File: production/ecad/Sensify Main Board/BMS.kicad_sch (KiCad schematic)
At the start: 76 parts, among them J1 1-2834011-3, J2 1-2834011-2, Q1 2N700, Q2 PMPB13XNE,115, Q3 PMPB13XNE,115, Q4 BSS223PWH6327XTSA1, U1 MAX17320G22, U2 BQ25306RTER, U3 LD29150DT33R, U4 LM22676MRX-5.0_NOPB

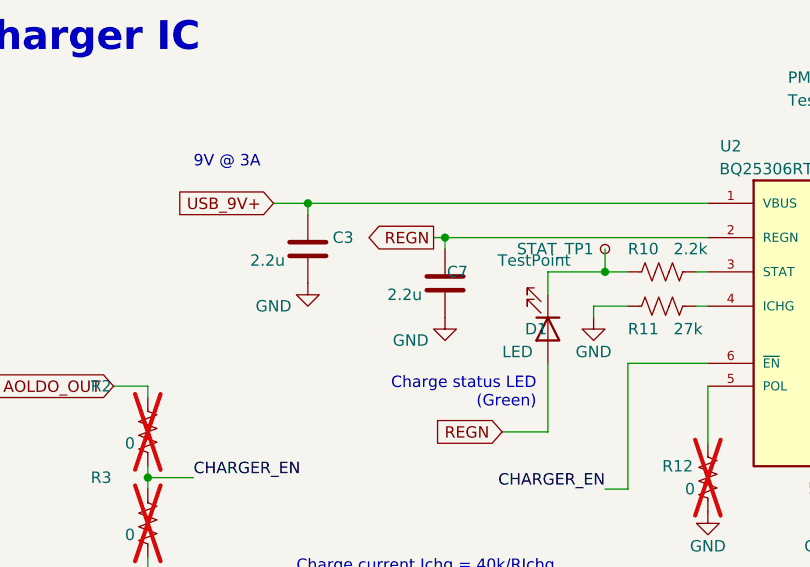
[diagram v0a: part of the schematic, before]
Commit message: added C16 footprint BMS
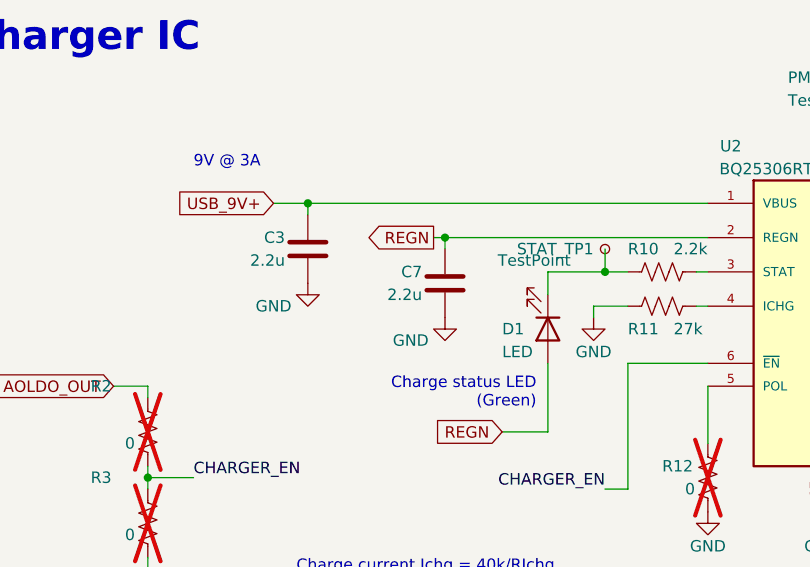
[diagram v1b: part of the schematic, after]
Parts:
- C16: footprint (none) -> Capacitor_SMD:C_0603_1608Metric_Pad1.08x0.95mm_HandSolder
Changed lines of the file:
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@@
   (symbol (lib_id "Device:C") (at 53.34 200.66 0) (unit 1)
     (in_bom yes) (on_board yes) (dnp no)
-    (property "Reference" "C3" (at 58.42 199.39 0)
+    (property "Reference" "C3" (at 50.8 199.39 0)
       (effects (font (size 1.27 1.27)) (justify right))
     )
@@
       (effects (font (size 1.27 1.27)) (justify right))
     )
-    (property "Footprint" "" (at 237.1852 209.55 0)
+    (property "Footprint" "Capacitor_SMD:C_0603_1608Metric_Pad1.08x0.95mm_HandSolder" (at 237.1852 209.55 0)
       (effects (font (size 1.27 1.27)) hide)
     )
@@
   (symbol (lib_id "Device:LED") (at 80.01 209.55 270) (unit 1)
     (in_bom yes) (on_board yes) (dnp no)
-    (property "Reference" "D1" (at 77.47 209.55 90)
+    (property "Reference" "D1" (at 74.93 209.55 90)
       (effects (font (size 1.27 1.27)) (justify left))
     )
@@
   (symbol (lib_id "Device:C") (at 68.58 204.47 0) (unit 1)
     (in_bom yes) (on_board yes) (dnp no)
-    (property "Reference" "C7" (at 71.12 203.2 0)
-      (effects (font (size 1.27 1.27)) (justify right))
-    )
+    (property "Reference" "C7" (at 66.04 203.2 0)
+      (effects (font (size 1.27 1.27)) (justify right))
+    )

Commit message: updated footprints for U3, U4
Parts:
- U3: footprint BMS:DPAK456P972X240-3N -> Sensify Footprints:DPAK456P972X240-3N
- U4: footprint LM22676MRX-5.0_NOPB:VREG_LM5017MR_NOPB -> Sensify Footprints:VREG_LM5017MR_NOPB
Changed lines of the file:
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@@
       (effects (font (size 1.27 1.27)))
     )
-    (property "Footprint" "LM22676MRX-5.0_NOPB:VREG_LM5017MR_NOPB" (at 303.53 115.57 0)
+    (property "Footprint" "Sensify Footprints:VREG_LM5017MR_NOPB" (at 303.53 115.57 0)
       (effects (font (size 1.27 1.27)) (justify bottom) hide)
     )
@@
       (effects (font (size 1.27 1.27)))
     )
-    (property "Footprint" "BMS:DPAK456P972X240-3N" (at 256.54 203.2 0)
+    (property "Footprint" "Sensify Footprints:DPAK456P972X240-3N" (at 256.54 203.2 0)
       (effects (font (size 1.27 1.27)) (justify bottom) hide)
     )

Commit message: reannotated REFDES
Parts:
- renumbered C7 to C6, C6 to C7

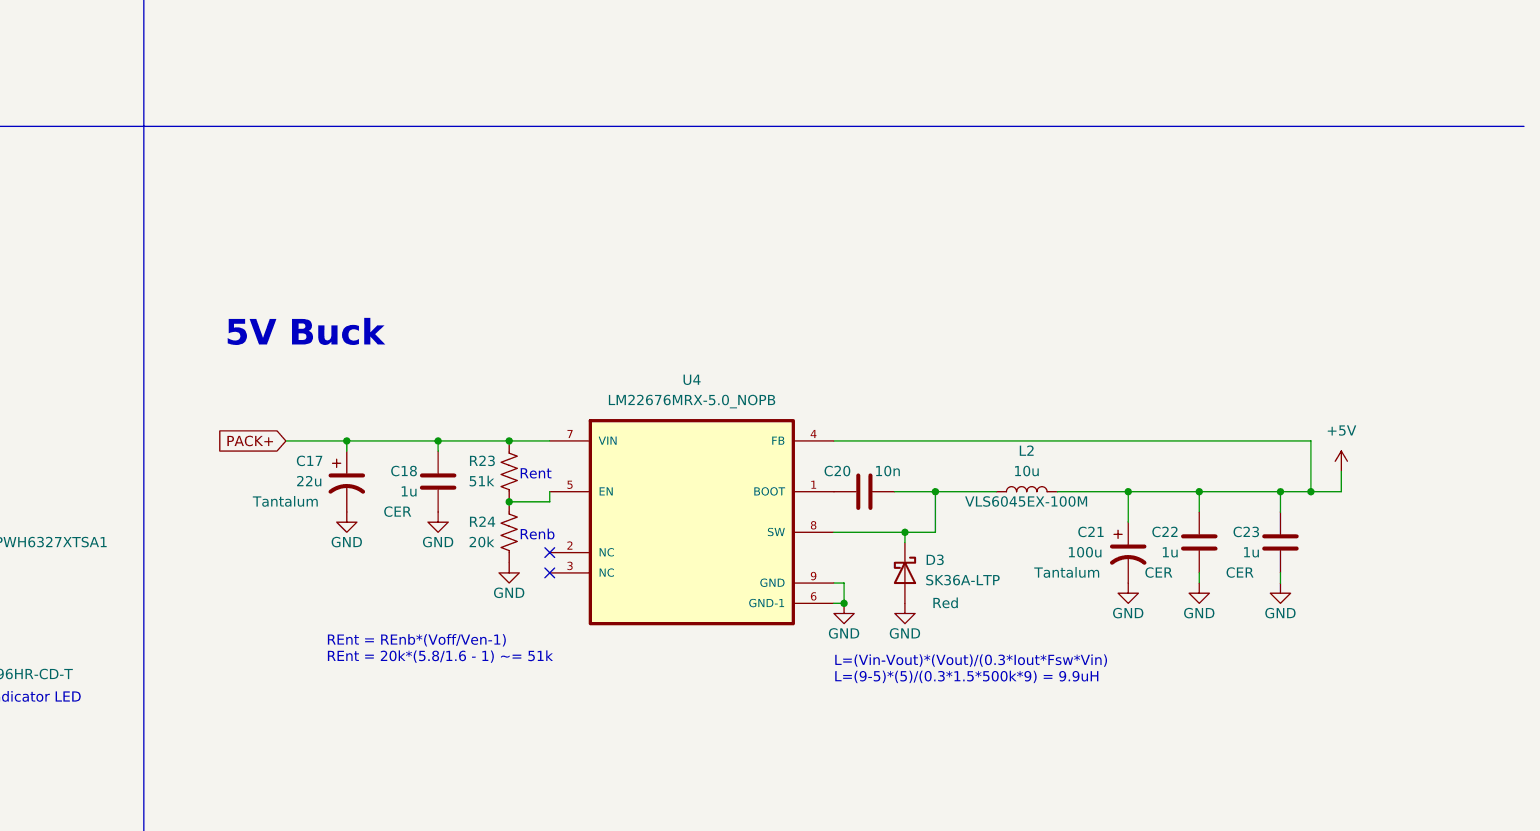
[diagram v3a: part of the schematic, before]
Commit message: added kill switch to BMS
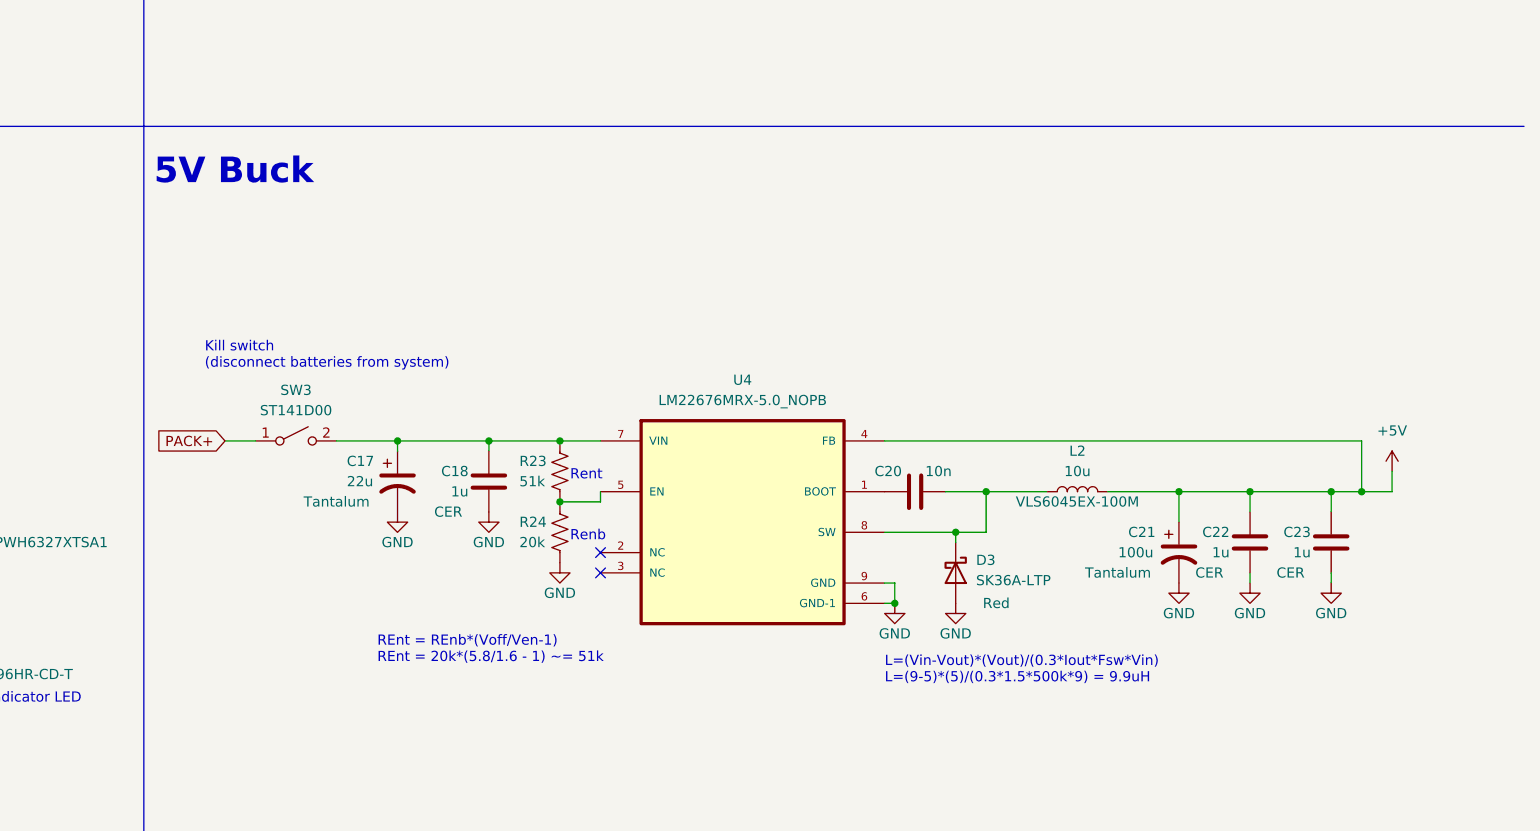
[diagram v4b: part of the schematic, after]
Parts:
- added SW3: ST141D00, Sensify Footprints:SW_ST141D00, symbol Switch:SW_SPST
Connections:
- net PACK+: now also SW3.1 (A); no longer C17.1, C18.1, R23.1, U4.7 (VIN)
- new net: C17.1, C18.1, R23.1, SW3.2 (B), U4.7 (VIN)
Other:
- note added: "Kill switch (disconnect batteries from system)"
- moved on the sheet: C17, C18, C20, C21, C22, C23, D3, L2, R23, R24, U4

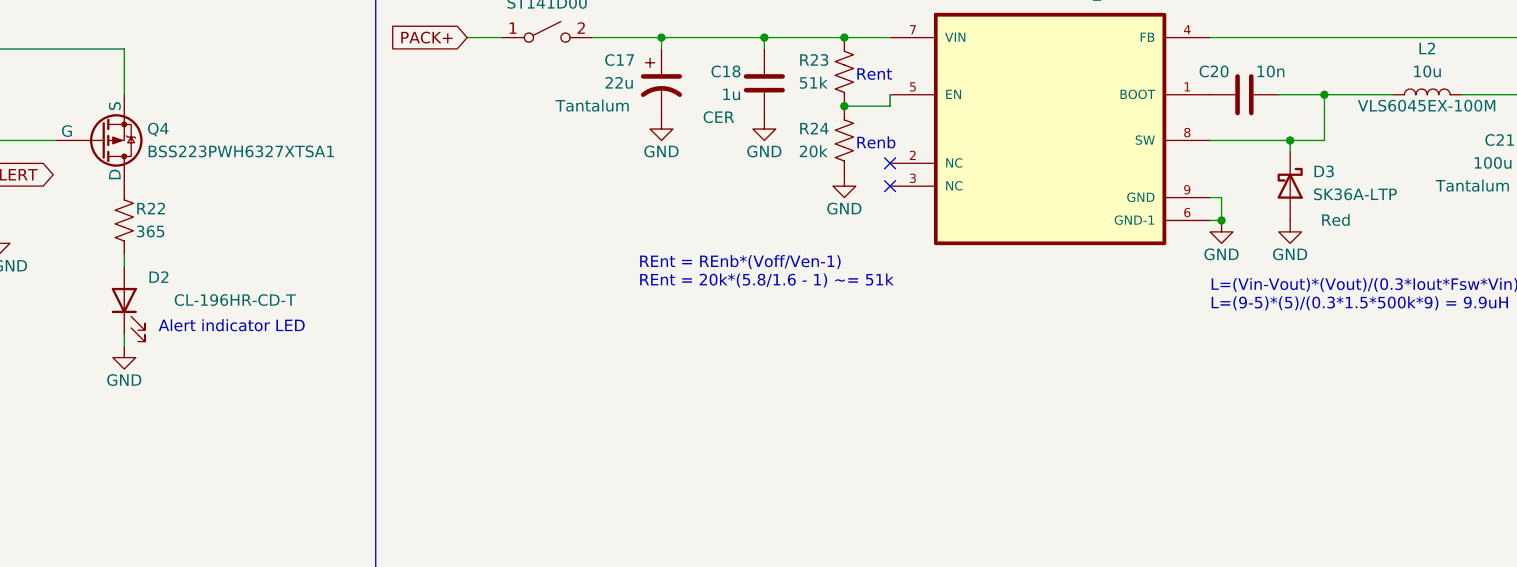
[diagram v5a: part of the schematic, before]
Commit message: continued main board layout
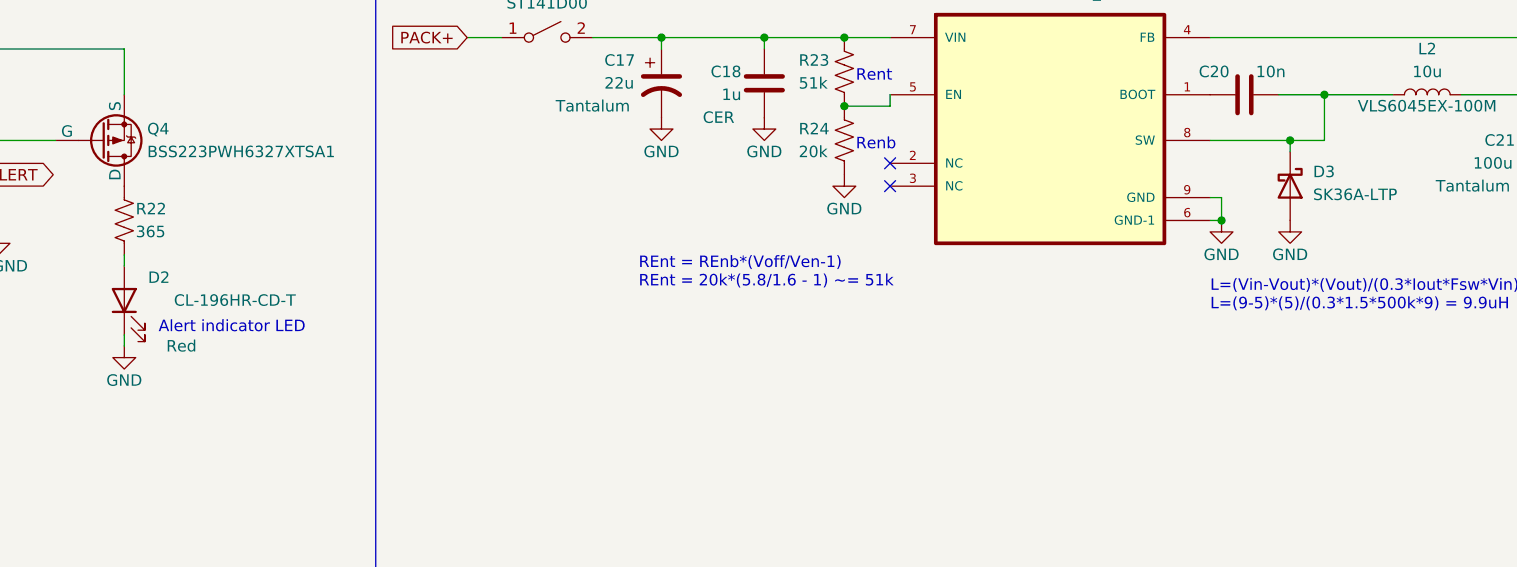
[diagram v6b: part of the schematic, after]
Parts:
- D2: Color (none) -> Red
- D3: Color Red -> (none)
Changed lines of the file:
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@@
       (effects (font (size 1.27 1.27)))
     )
-    (property "Color" "Red" (at 341.63 125.73 90)
-      (effects (font (size 1.27 1.27)))
+    (property "Color" "" (at 341.63 125.73 90)
+      (effects (font (size 1.27 1.27)) hide)
     )
     (pin "2")
@@
       (effects (font (size 1.27 1.27)) hide)
     )
-    (pin "2")
+    (property "Color" "Red" (at 213.36 139.7 90)
+      (effects (font (size 1.27 1.27)))
+    )
+    (pin "2")

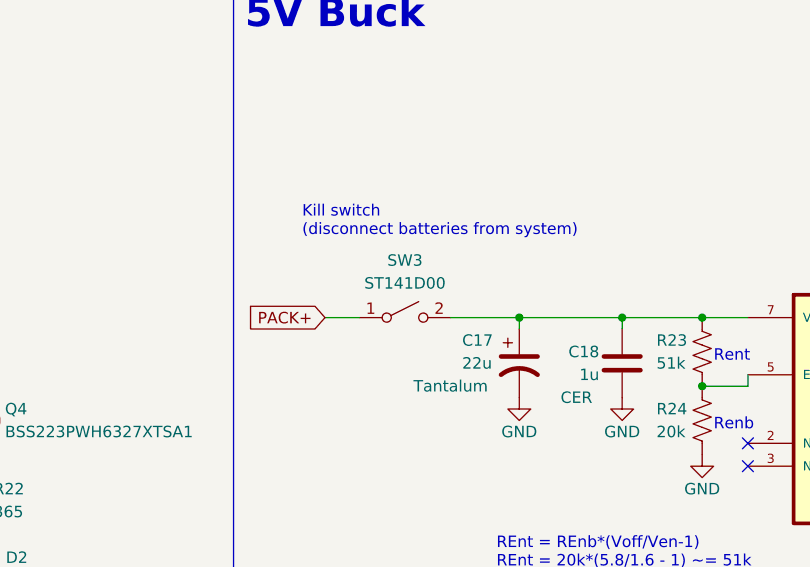
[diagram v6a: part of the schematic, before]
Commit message: slightly smaller switch added
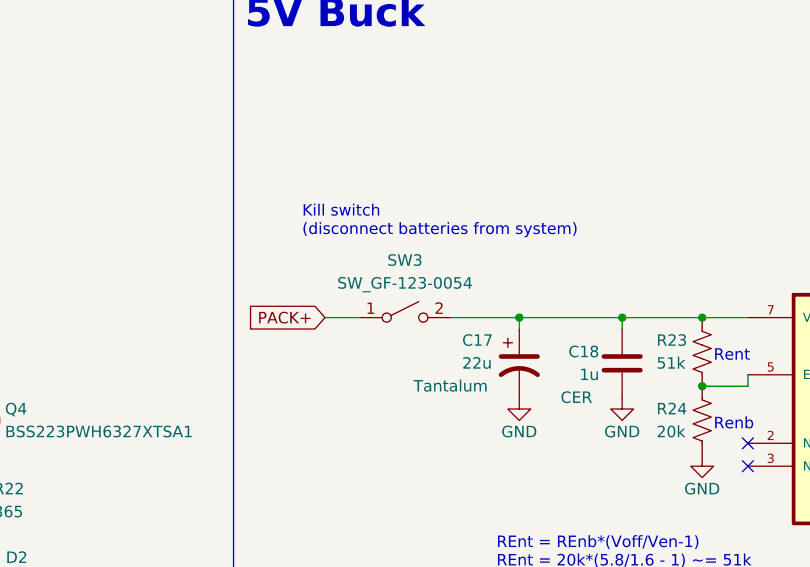
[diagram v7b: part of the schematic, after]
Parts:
- SW3: value ST141D00 -> SW_GF-123-0054; footprint Sensify Footprints:SW_ST141D00 -> Sensify Footprints:SW_GF-123-0054; Link https://www.digikey.com/en/products/detail/e-switch/ST141D0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 -> (none)
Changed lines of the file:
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@@
       (effects (font (size 1.27 1.27)))
     )
-    (property "Value" "ST141D00" (at 254 101.6 0)
+    (property "Value" "SW_GF-123-0054" (at 254 101.6 0)
       (effects (font (size 1.27 1.27)))
     )
-    (property "Footprint" "Sensify Footprints:SW_ST141D00" (at 254 105.41 0)
+    (property "Footprint" "Sensify Footprints:SW_GF-123-0054" (at 254 105.41 0)
       (effects (font (size 1.27 1.27)) hide)
     )
-    (property "Datasheet" "https://configured-product-images.s3.amazonaws.com/Datasheets/ST1.pdf" (at 254 105.41 0)
+    (property "Datasheet" "SW_GF-123-0054" (at 254 105.41 0)
       (effects (font (size 1.27 1.27)) hide)
     )
-    (property "Link" "https://www.digikey.com/en/products/detail/e-switch/ST141D00/2116289" (at 254 105.41 0)
-      (effects (font (size 1.27 1.27)) hide)
-    )

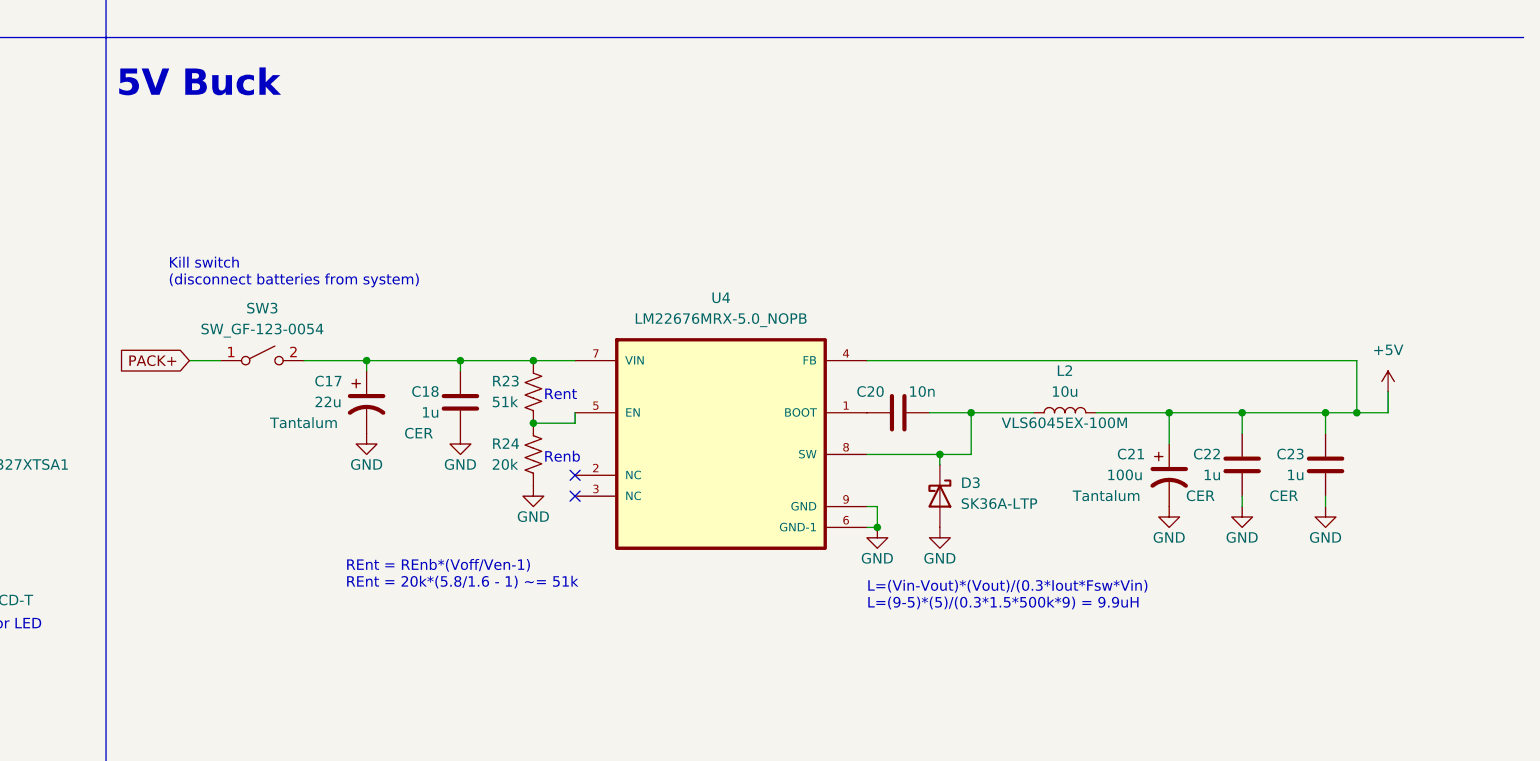
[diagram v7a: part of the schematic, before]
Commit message: smaller switch
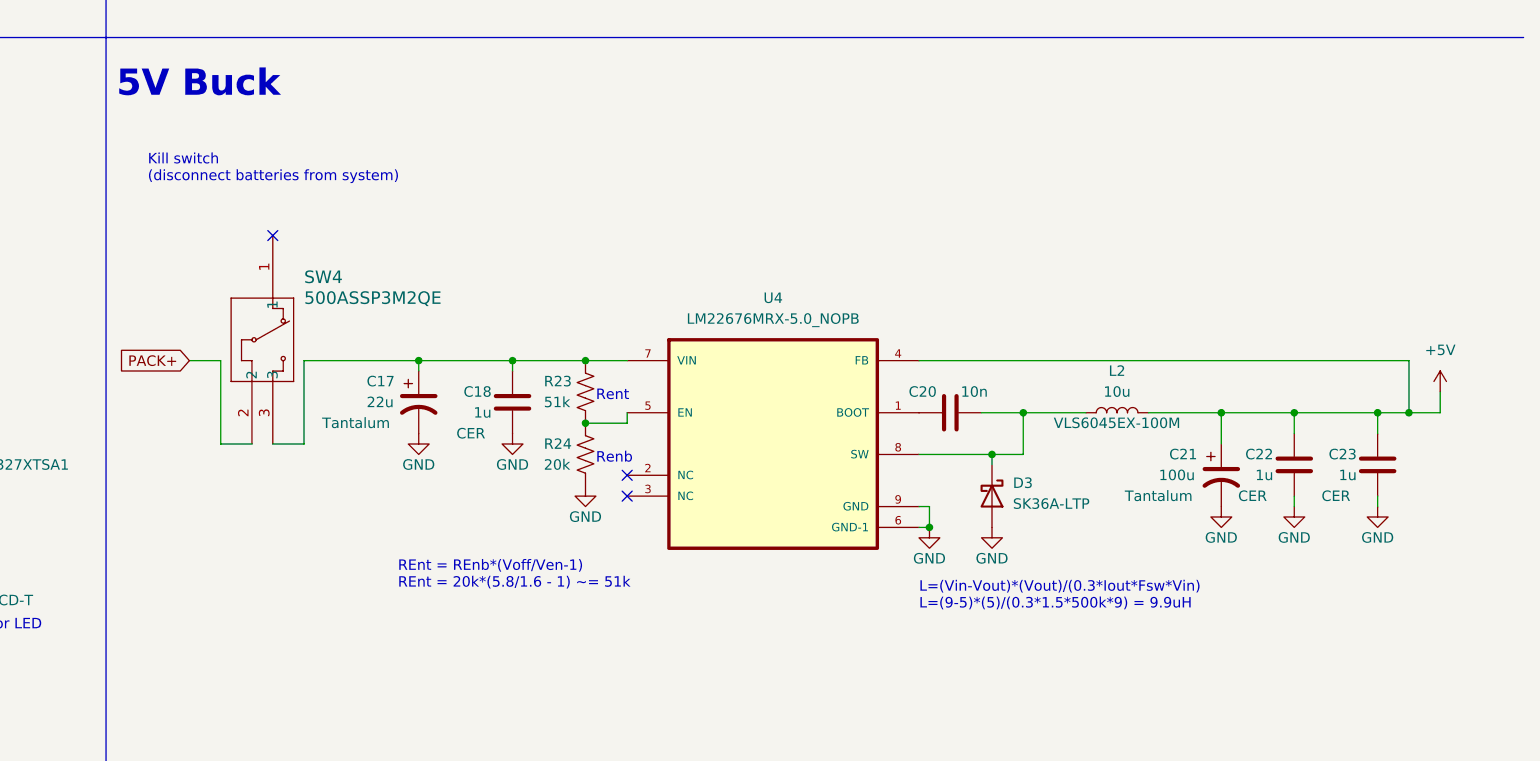
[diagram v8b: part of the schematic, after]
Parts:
- removed SW3: SW_GF-123-0054, Sensify Footprints:SW_GF-123-0054, symbol Switch:SW_SPST
- added SW4: 500ASSP3M2QE, 500ASSP3M2QE_EWI, symbol BMS:500ASSP3M2QE
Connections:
- net PACK+: now also SW4.2
- net at C17.1, C18.1, R23.1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: now also SW4.3
- no-connect marks 5 -> 6
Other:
- moved on the sheet: C17, C18, C20, C21, C22, C23, D3, L2, R23, R24, U4
